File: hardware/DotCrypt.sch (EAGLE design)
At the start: 7 parts, among them CN1 1X4-BIG, U1 ATMEGA328P-MU-QFN32, U3 ATSHA204-TSU

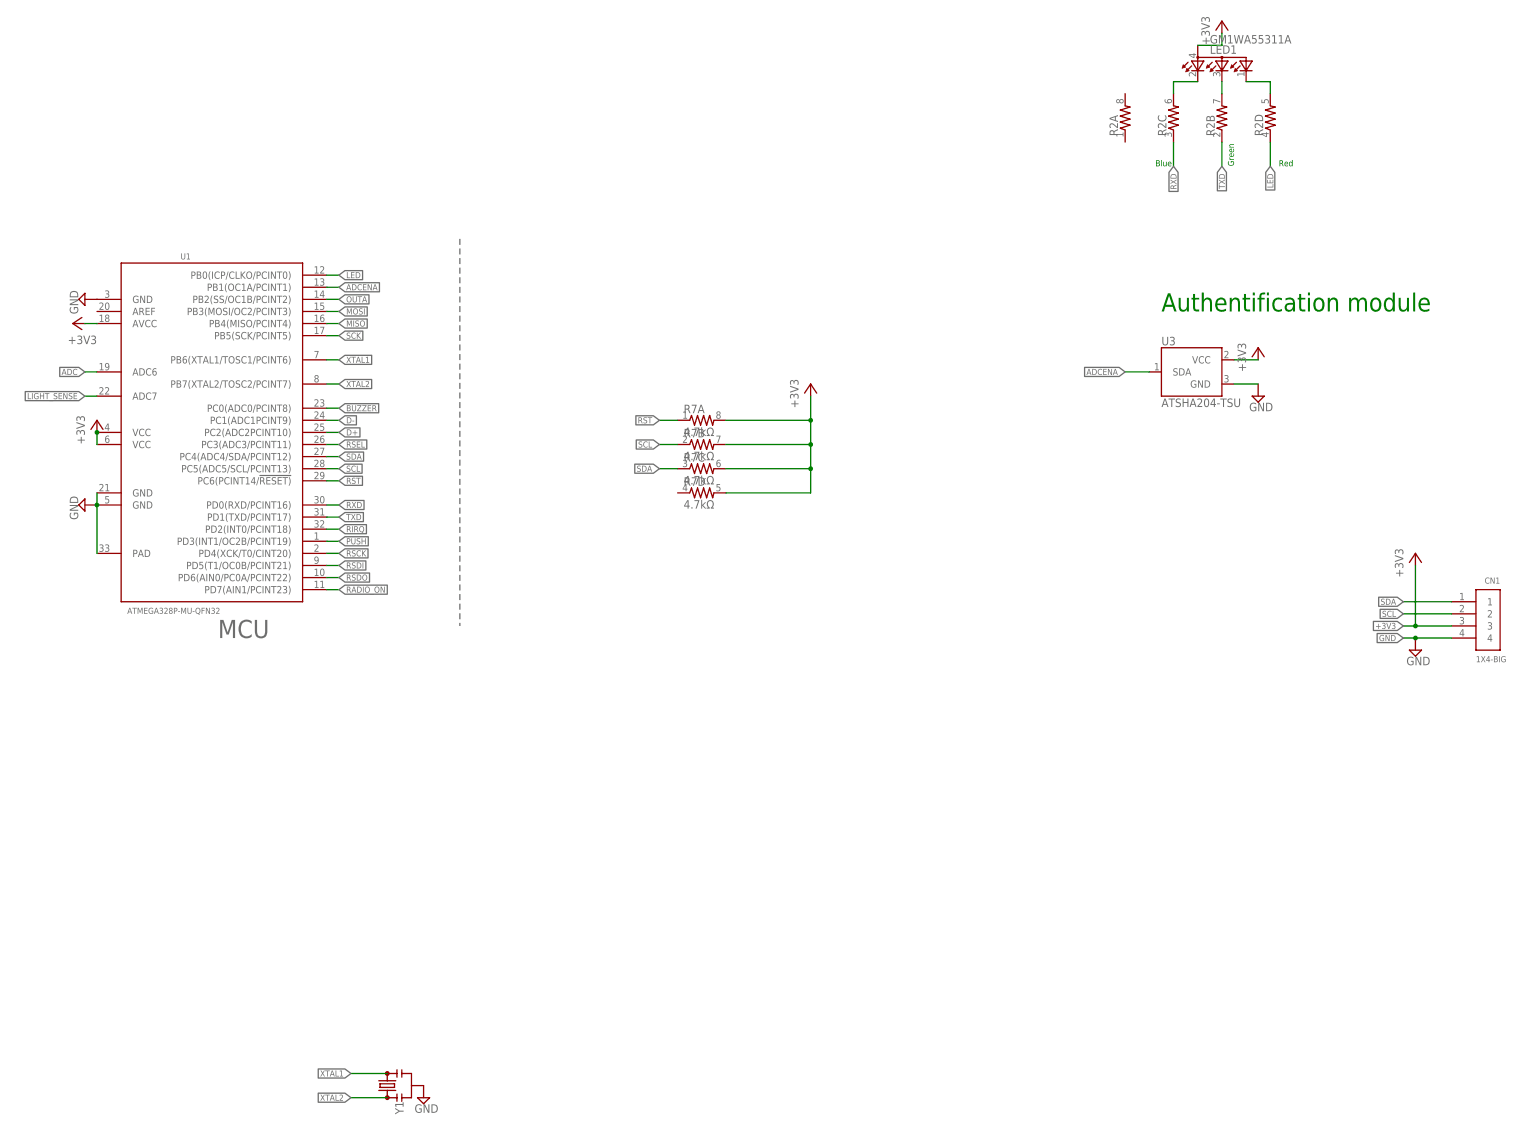
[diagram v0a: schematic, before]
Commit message: Overlapping I2C & UART pins
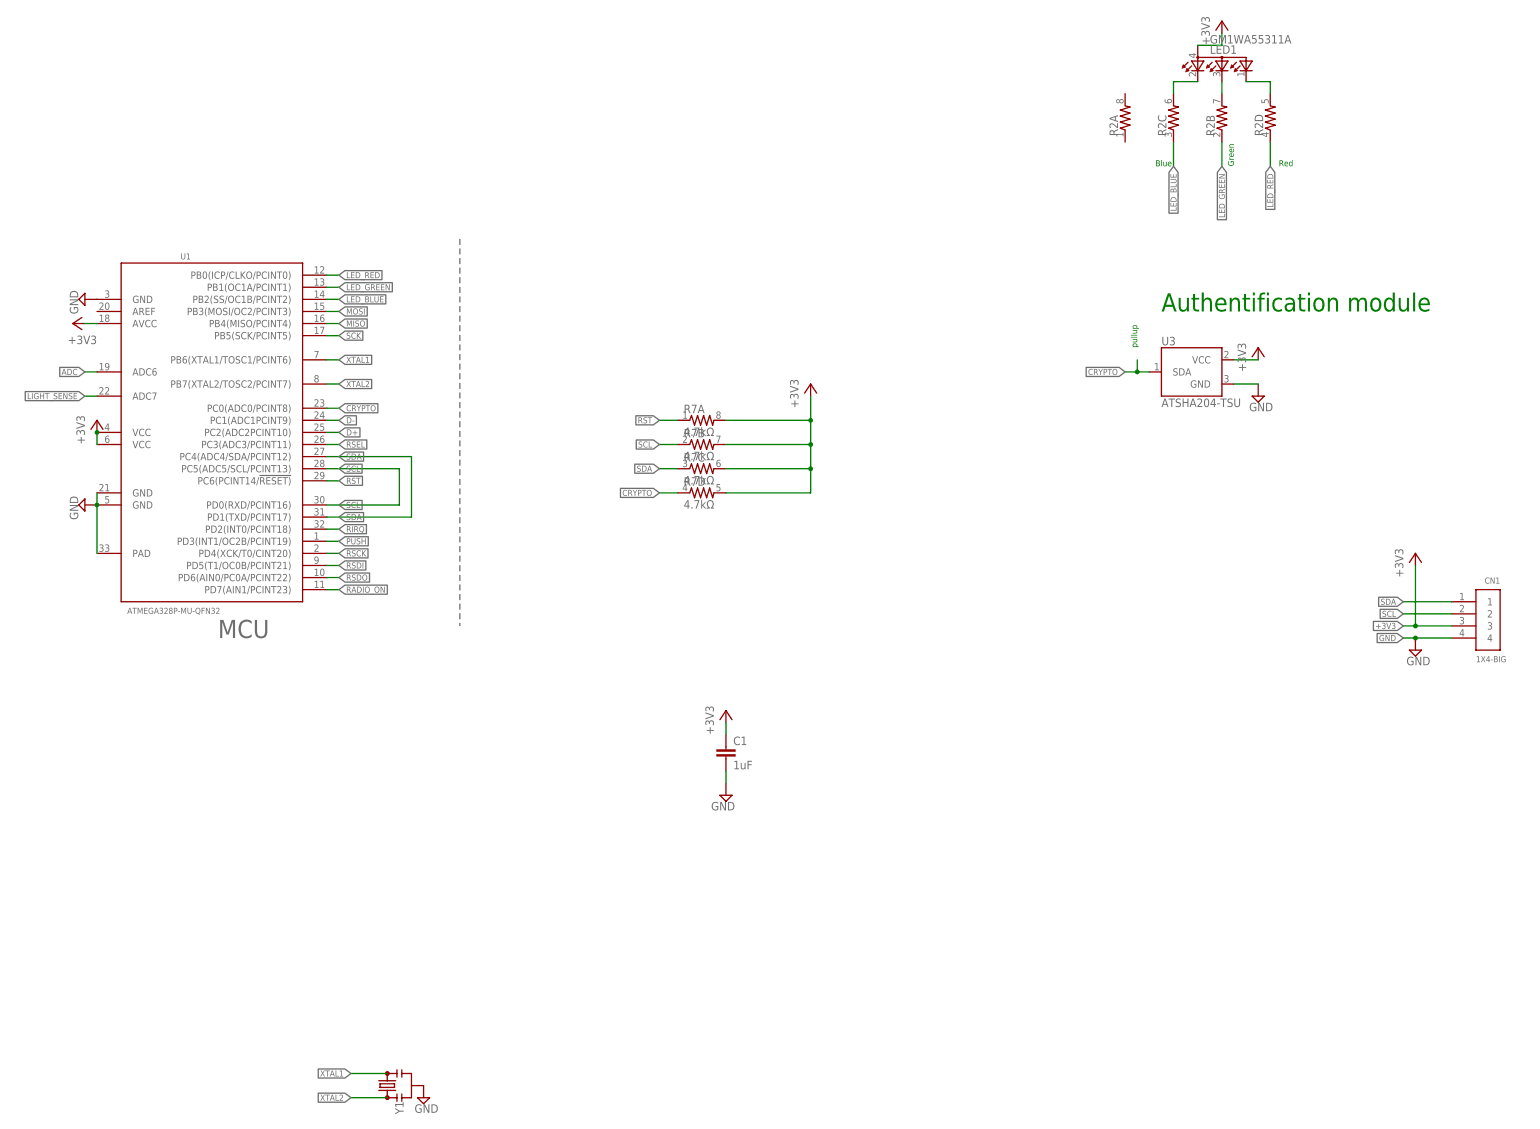
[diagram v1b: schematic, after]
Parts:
- added C1: 1uF, rcl:C-EUC0603
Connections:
- net LED renamed LED_RED
- removed net ADCENA: U1.PB1(OC1A/PCINT1), U3.SDA
- removed net BUZZER: U1.PC0(ADC0/PCINT8)
- removed net OUTA: U1.PB2(SS/OC1B/PCINT2)
- removed net RXD: R2C.1, U1.PD0(RXD/PCINT16)
- removed net TXD: R2B.1, U1.PD1(TXD/PCINT17)
- new net CRYPTO: R7D.1, U1.PC0(ADC0/PCINT8), U3.SDA
- new net LED_BLUE: R2C.1, U1.PB2(SS/OC1B/PCINT2)
- new net LED_GREEN: R2B.1, U1.PB1(OC1A/PCINT1)
- net +3V3: now also C1.1
- net GND: now also C1.2
- net SCL: now also U1.PD0(RXD/PCINT16)
- net SDA: now also U1.PD1(TXD/PCINT17)
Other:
- note added: "pullup"
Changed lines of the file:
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@@
 <setting verticaltext="up"/>
 </settings>
-<grid distance="0.1" unitdist="inch" unit="inch" style="lines" multiple="1" display="no" altdistance="0.01" altunitdist="inch" altunit="inch"/>
+<grid distance="0.05" unitdist="inch" unit="inch" style="lines" multiple="1" display="no" altdistance="0.01" altunitdist="inch" altunit="inch"/>
 <layers>
 <layer number="1" name="Top" color="4" fill="1" visible="no" active="no"/>
@@
 <part name="Y1" library="SparkFun-Clocks" deviceset="RESONATOR" device="SMD-3.2X1.3"/>
 <part name="SUPPLY30" library="supply2" deviceset="GND" device=""/>
+<part name="SUPPLY27" library="supply2" deviceset="GND" device=""/>
+<part name="+3V19" library="supply1" deviceset="+3V3" device=""/>
+<part name="C1" library="rcl" deviceset="C-EU" device="C0603" value="1uF"/>
 </parts>
 <sheets>
@@
 <text x="250.698" y="193.04" size="1.27" layer="91">Red</text>
 <text x="226.06" y="162.56" size="3.81" layer="91">Authentification module</text>
+<text x="220.98" y="154.94" size="1.27" layer="91" rot="R90">pullup</text>
 </plain>
 <instances>
@@
 <instance part="Y1" gate="G$1" x="63.5" y="0" rot="R90"/>
 <instance part="SUPPLY30" gate="GND" x="71.12" y="-2.54"/>
+<instance part="SUPPLY27" gate="GND" x="134.62" y="60.96" rot="MR0"/>
+<instance part="+3V19" gate="G$1" x="134.62" y="78.74"/>
+<instance part="C1" gate="G$1" x="134.62" y="71.12"/>
 </instances>
 <busses>
@@
 <pinref part="SUPPLY30" gate="GND" pin="GND"/>
 </segment>
+<segment>
+<pinref part="SUPPLY27" gate="GND" pin="GND"/>
+<pinref part="C1" gate="G$1" pin="2"/>
+<wire x1="134.62" y1="63.5" x2="134.62" y2="66.04" width="0.1524" layer="91"/>
+</segment>
 </net>
 <net name="SCK" class="0">
@@
 <segment>
 <pinref part="U1" gate="G$1" pin="PC4(ADC4/SDA/PCINT12)"/>
-<wire x1="50.8" y1="132.08" x2="53.34" y2="132.08" width="0.1524" layer="91"/>
 <label x="53.34" y="132.08" size="1.27" layer="95" xref="yes"/>
+<wire x1="50.8" y1="132.08" x2="68.58" y2="132.08" width="0.1524" layer="91"/>
+<wire x1="68.58" y1="132.08" x2="68.58" y2="119.38" width="0.1524" layer="91"/>
+<pinref part="U1" gate="G$1" pin="PD1(TXD/PCINT17)"/>
+<label x="53.34" y="119.38" size="1.27" layer="95" xref="yes"/>
+<wire x1="68.58" y1="119.38" x2="50.8" y2="119.38" width="0.1524" layer="91"/>
 </segment>
 <segment>
@@
 <segment>
 <pinref part="U1" gate="G$1" pin="PC5(ADC5/SCL/PCINT13)"/>
-<wire x1="50.8" y1="129.54" x2="53.34" y2="129.54" width="0.1524" layer="91"/>
 <label x="53.34" y="129.54" size="1.27" layer="95" xref="yes"/>
+<wire x1="50.8" y1="129.54" x2="66.04" y2="129.54" width="0.1524" layer="91"/>
+<wire x1="66.04" y1="129.54" x2="66.04" y2="121.92" width="0.1524" layer="91"/>
+<pinref part="U1" gate="G$1" pin="PD0(RXD/PCINT16)"/>
+<label x="53.34" y="121.92" size="1.27" layer="95" xref="yes"/>
+<wire x1="66.04" y1="121.92" x2="50.8" y2="121.92" width="0.1524" layer="91"/>
 </segment>
 <segment>
@@
 <pinref part="+3V10" gate="G$1" pin="+3V3"/>
 </segment>
+<segment>
+<pinref part="+3V19" gate="G$1" pin="+3V3"/>
+<wire x1="134.62" y1="76.2" x2="134.62" y2="73.66" width="0.1524" layer="91"/>
+<pinref part="C1" gate="G$1" pin="1"/>
+</segment>
 </net>
 <net name="PUSH" class="0">
@@
 </segment>
 </net>
-<net name="LED" class="0">
-<segment>
-<pinref part="U1" gate="G$1" pin="PB0(ICP/CLKO/PCINT0)"/>
-<wire x1="50.8" y1="170.18" x2="53.34" y2="170.18" width="0.1524" layer="91"/>
-<label x="53.34" y="170.18" size="1.27" layer="95" xref="yes"/>
-</segment>
-<segment>
-<wire x1="248.92" y1="198.12" x2="248.92" y2="193.04" width="0.1524" layer="91"/>
-<label x="248.92" y="193.04" size="1.27" layer="95" rot="R270" xref="yes"/>
-<pinref part="R2" gate="D" pin="1"/>
-</segment>
-</net>
 <net name="LIGHT_SENSE" class="0">
 <segment>
@@
 </segment>
 </net>
-<net name="ADCENA" class="0">
-<segment>
-<pinref part="U1" gate="G$1" pin="PB1(OC1A/PCINT1)"/>
-<wire x1="50.8" y1="167.64" x2="53.34" y2="167.64" width="0.1524" layer="91"/>
-<label x="53.34" y="167.64" size="1.27" layer="95" xref="yes"/>
-</segment>
-<segment>
-<pinref part="U3" gate="G$1" pin="SDA"/>
-<wire x1="223.52" y1="149.86" x2="218.44" y2="149.86" width="0.1524" layer="91"/>
-<label x="218.44" y="149.86" size="1.27" layer="95" rot="R180" xref="yes"/>
-</segment>
-</net>
-<net name="TXD" class="0">
-<segment>
-<pinref part="U1" gate="G$1" pin="PD1(TXD/PCINT17)"/>
-<wire x1="50.8" y1="119.38" x2="53.34" y2="119.38" width="0.1524" layer="91"/>
-<label x="53.34" y="119.38" size="1.27" layer="95" xref="yes"/>
-</segment>
-<segment>
-<wire x1="238.76" y1="198.12" x2="238.76" y2="193.04" width="0.1524" layer="91"/>
-<label x="238.76" y="193.04" size="1.27" layer="95" rot="R270" xref="yes"/>
-<pinref part="R2" gate="B" pin="1"/>
-</segment>
-</net>
-<net name="RXD" class="0">
-<segment>
-<pinref part="U1" gate="G$1" pin="PD0(RXD/PCINT16)"/>
-<wire x1="50.8" y1="121.92" x2="53.34" y2="121.92" width="0.1524" layer="91"/>
-<label x="53.34" y="121.92" size="1.27" layer="95" xref="yes"/>
-</segment>
-<segment>
-<wire x1="228.6" y1="198.12" x2="228.6" y2="193.04" width="0.1524" layer="91"/>
-<label x="228.6" y="193.04" size="1.27" layer="95" rot="R270" xref="yes"/>
-<pinref part="R2" gate="C" pin="1"/>
-</segment>
-</net>
 <net name="ADC" class="0">
 <segment>
@@
 </segment>
 </net>
-<net name="BUZZER" class="0">
+<net name="CRYPTO" class="0">
 <segment>
 <pinref part="U1" gate="G$1" pin="PC0(ADC0/PCINT8)"/>
@@
 <label x="53.34" y="142.24" size="1.27" layer="95" xref="yes"/>
 </segment>
-</net>
-<net name="OUTA" class="0">
-<segment>
-<pinref part="U1" gate="G$1" pin="PB2(SS/OC1B/PCINT2)"/>
-<wire x1="50.8" y1="165.1" x2="53.34" y2="165.1" width="0.1524" layer="91"/>
-<label x="53.34" y="165.1" size="1.27" layer="95" xref="yes"/>
+<segment>
+<pinref part="U3" gate="G$1" pin="SDA"/>
+<wire x1="223.52" y1="149.86" x2="220.98" y2="149.86" width="0.1524" layer="91"/>
+<label x="218.44" y="149.86" size="1.27" layer="95" rot="R180" xref="yes"/>
+<wire x1="220.98" y1="149.86" x2="218.44" y2="149.86" width="0.1524" layer="91"/>
+<wire x1="220.98" y1="152.4" x2="220.98" y2="149.86" width="0.1524" layer="91"/>
+<junction x="220.98" y="149.86"/>
+</segment>
+<segment>
+<pinref part="R7" gate="D" pin="1"/>
+<wire x1="124.46" y1="124.46" x2="120.65" y2="124.46" width="0.1524" layer="91"/>
+<label x="120.65" y="124.46" size="1.27" layer="95" rot="R180" xref="yes"/>
 </segment>
 </net>
@@
 </segment>
 </net>
+<net name="LED_RED" class="0">
+<segment>
+<pinref part="U1" gate="G$1" pin="PB0(ICP/CLKO/PCINT0)"/>
+<wire x1="50.8" y1="170.18" x2="53.34" y2="170.18" width="0.1524" layer="91"/>
+<label x="53.34" y="170.18" size="1.27" layer="95" xref="yes"/>
+</segment>
+<segment>
+<wire x1="248.92" y1="198.12" x2="248.92" y2="193.04" width="0.1524" layer="91"/>
+<label x="248.92" y="193.04" size="1.27" layer="95" rot="R270" xref="yes"/>
+<pinref part="R2" gate="D" pin="1"/>
+</segment>
+</net>
+<net name="LED_GREEN" class="0">
+<segment>
+<pinref part="U1" gate="G$1" pin="PB1(OC1A/PCINT1)"/>
+<wire x1="50.8" y1="167.64" x2="53.34" y2="167.64" width="0.1524" layer="91"/>
+<label x="53.34" y="167.64" size="1.27" layer="95" xref="yes"/>
+</segment>
+<segment>
+<pinref part="R2" gate="B" pin="1"/>
+<wire x1="238.76" y1="198.12" x2="238.76" y2="193.04" width="0.1524" layer="91"/>
+<label x="238.76" y="193.04" size="1.27" layer="95" rot="R270" xref="yes"/>
+</segment>
+</net>
+<net name="LED_BLUE" class="0">
+<segment>
+<pinref part="R2" gate="C" pin="1"/>
+<wire x1="228.6" y1="198.12" x2="228.6" y2="193.04" width="0.1524" layer="91"/>
+<label x="228.6" y="193.04" size="1.27" layer="95" rot="R270" xref="yes"/>
+</segment>
+<segment>
+<pinref part="U1" gate="G$1" pin="PB2(SS/OC1B/PCINT2)"/>
+<wire x1="50.8" y1="165.1" x2="53.34" y2="165.1" width="0.1524" layer="91"/>
+<label x="53.34" y="165.1" size="1.27" layer="95" xref="yes"/>
+</segment>
+</net>

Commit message: Add QR, sch structure lines
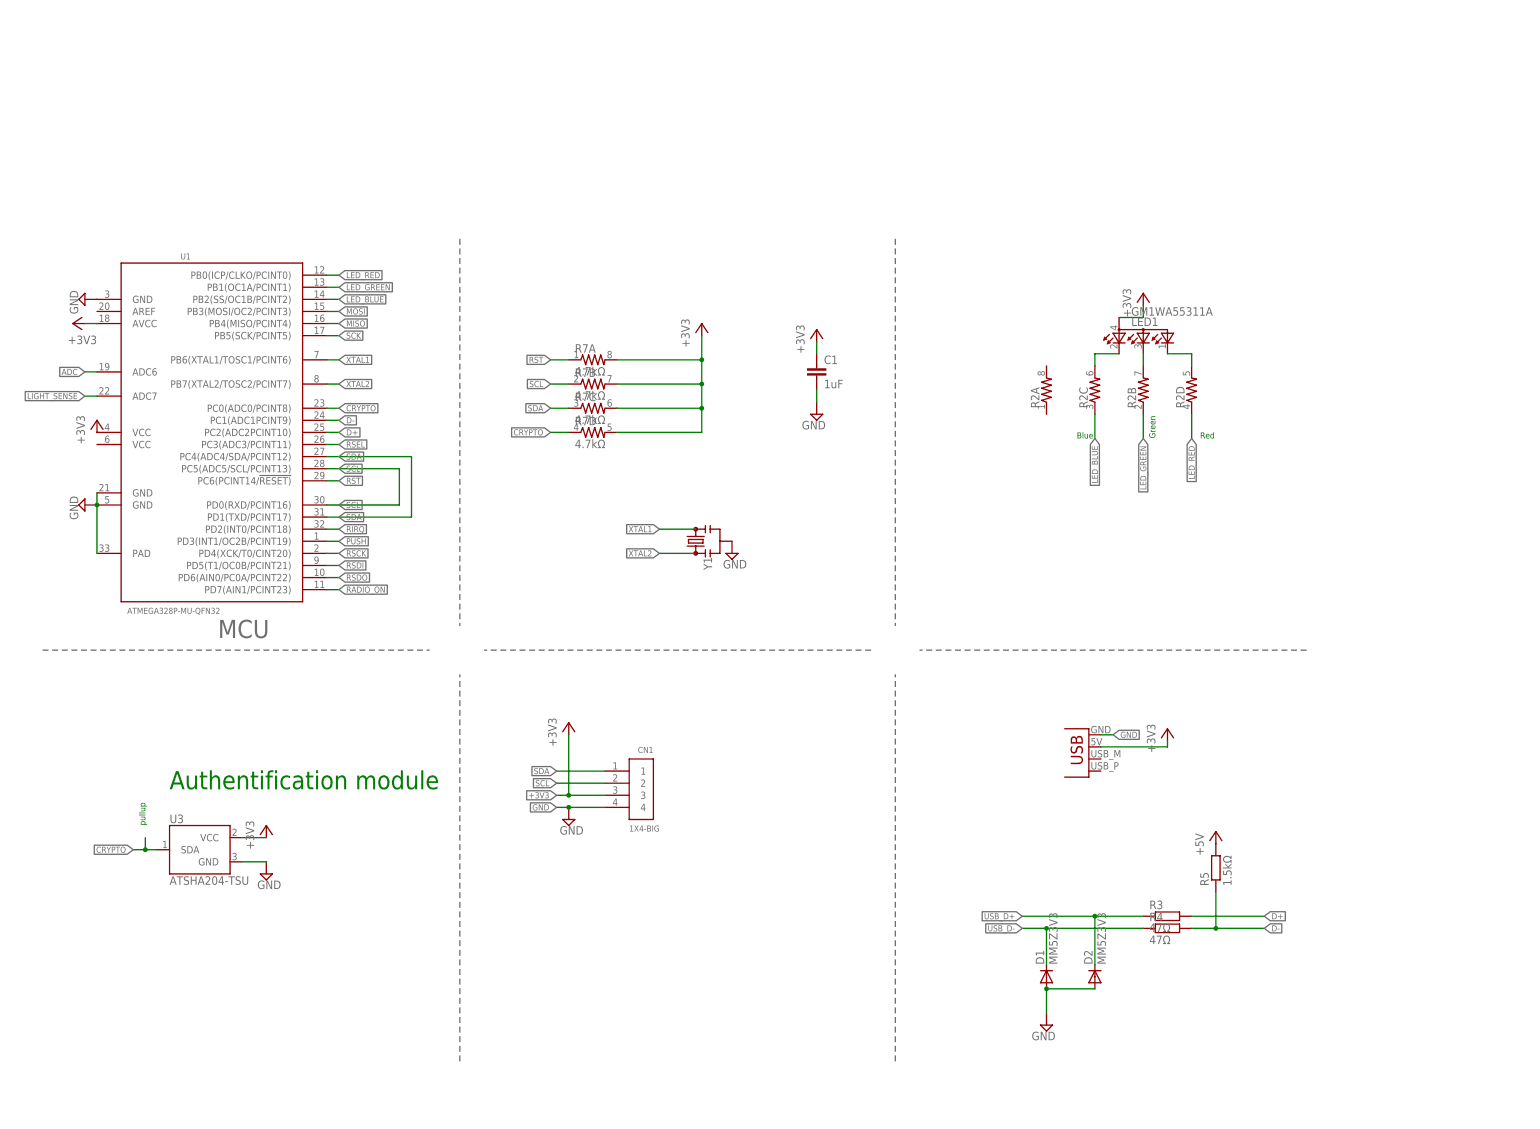
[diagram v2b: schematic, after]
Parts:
- added D1, D2: MM5Z3V3, diode:DIODE-SOD523
- added JP3: USBPCB, Spark:USBPCB
- added R3, R4: 47Ω, rcl:R-EU_R0603
- added R5: 1.5kΩ, rcl:R-EU_R0603
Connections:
- new net +5V: R5.2
- new net USB_D+: D2.C, R3.1
- new net USB_D-: D1.C, R4.1
- net +3V3: now also JP3.VBUS; no longer U1.VCC@2
- net D+: now also R3.2
- net D-: now also R4.2, R5.1
- net GND: now also D1.A, D2.A, JP3.GND
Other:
- moved on the sheet: C1, CN1, LED1, R2A, R2B, R2C, R2D, R7A, R7B, R7C, R7D, U3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
